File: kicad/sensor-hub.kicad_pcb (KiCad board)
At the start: 2 copper layers, 85 x 56 mm, 42 parts, among them J1 USB_B_Micro, J10 DHT22, J11 MQ_Sensors, J12 I2C-Si7021, J13 BG312L, J14 CC_DBG, J15 BT_DBG, J16 ZB_DBG, J17 CC_PWR, J5 ESP_TXD, J6 ESP_RXD, J7 DallasPullUp, J8 IRRecv/Dallas, J9 BH1750/Display, Q3 PN2222A, SW1 SW_Flash, U1 AP1117-33, U2 ESP-12F, U3 SZ1-CC2530, U5 CH330N

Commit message: Update kicad files
Signed-off-by: Zamir SUN <sztsian@gmail.com>
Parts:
- moved J10 6.22 mm to (277.7, 142.4)
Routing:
- net GND: track 203.9 -> 211.5 mm
- net DHT22: track 30.8 -> 37.0 mm
- net GPIO5: track 153.4 -> 156.3 mm
- net GPIO4: track 126.2 -> 129.0 mm
- net 3V3_MCU: track 386.4 -> 388.1 mm
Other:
- board text added: "Sensor Hub v0.3 by Zamir SUN"
- board text removed: "Sensor Hub v0.2 by Zamir SUN"

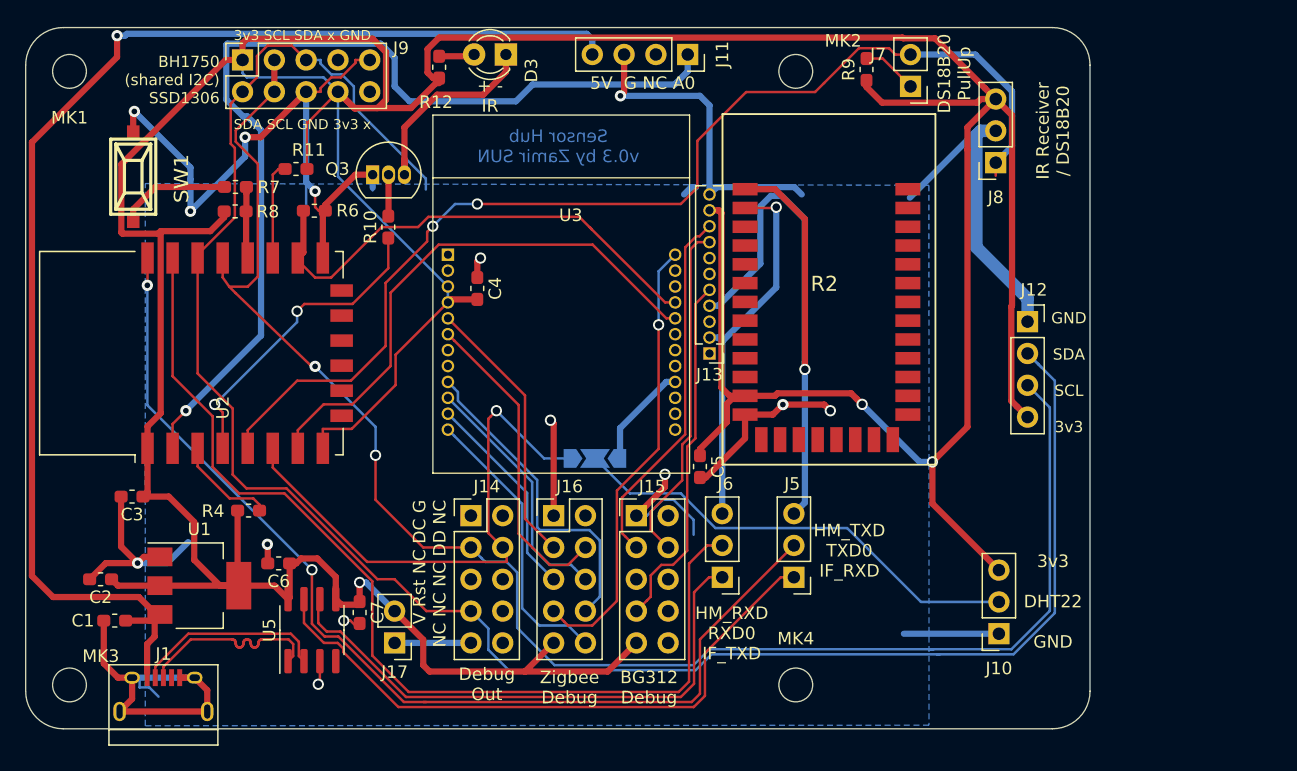
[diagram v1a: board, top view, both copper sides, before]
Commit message: WIP: v0.4 with pin order converter board
Signed-off-by: Zamir SUN <sztsian@gmail.com>
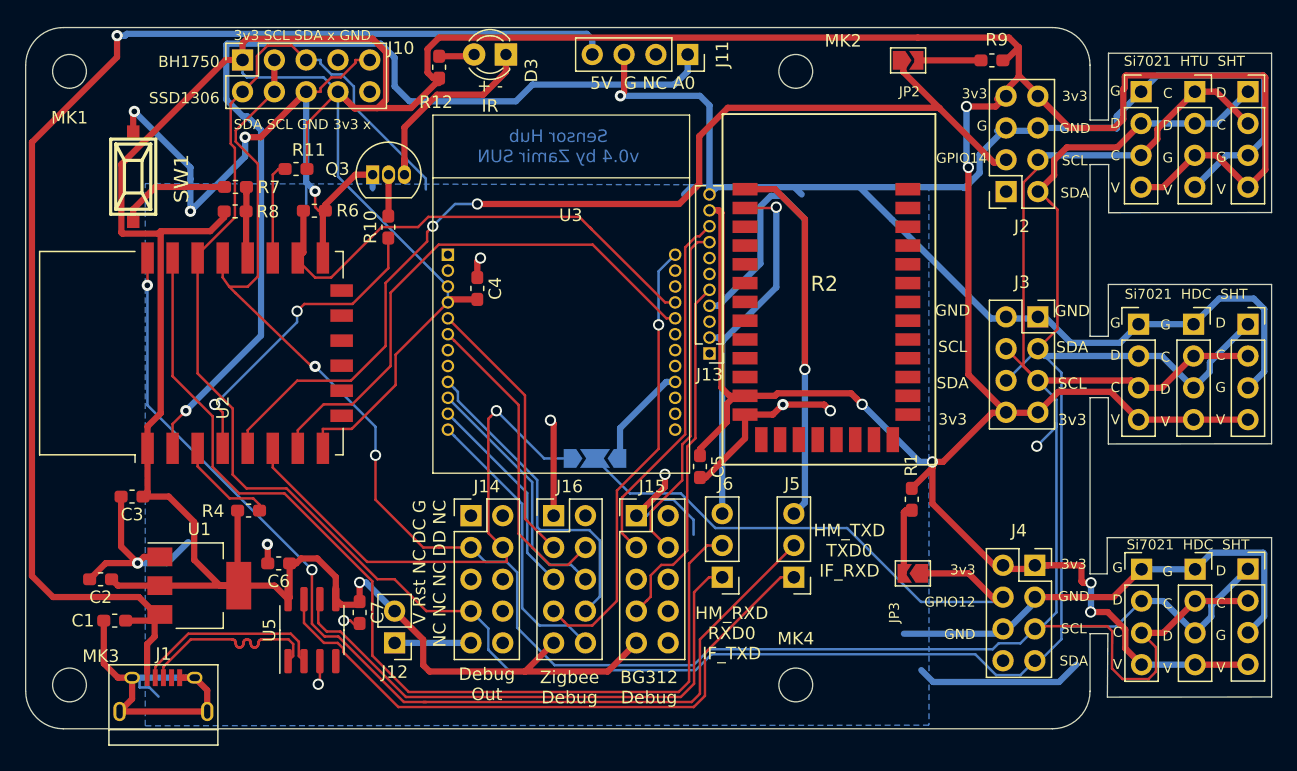
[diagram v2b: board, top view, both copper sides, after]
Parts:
- removed the J10 at (277.7, 142.4)
- removed the J12 at (280.0, 117.5)
- added J17: Si7021, Connector_PinHeader_2.54mm:PinHeader_1x04_P2.54mm_Vertical, F.Cu at (288.9, 117.7)
- added J18: HDC1080, Connector_PinSocket_2.54mm:PinSocket_1x04_P2.54mm_Vertical, F.Cu at (293.3, 117.7)
- added J19: SHT, Connector_PinSocket_2.54mm:PinSocket_1x04_P2.54mm_Vertical, F.Cu at (297.6, 117.7)
- added J2: IO14/SHT, Connector_PinSocket_2.54mm:PinSocket_2x04_P2.54mm_Vertical, F.Cu at (278.3, 107.1)
- added J20: Si7021, Connector_PinHeader_2.54mm:PinHeader_1x04_P2.54mm_Vertical, F.Cu at (289.1, 137.3)
- added J21: HDC1080, Connector_PinSocket_2.54mm:PinSocket_1x04_P2.54mm_Vertical, F.Cu at (293.4, 137.3)
- added J22: SHT, Connector_PinSocket_2.54mm:PinSocket_1x04_P2.54mm_Vertical, F.Cu at (297.6, 137.2)
- added J3: HDC/Si7021, Connector_PinSocket_2.54mm:PinSocket_2x04_P2.54mm_Vertical, F.Cu at (280.8, 117.1)
- added J4: IO12/SHT, Connector_PinSocket_2.54mm:PinSocket_2x04_P2.54mm_Vertical, F.Cu at (280.6, 136.9)
- added J9: SHT, Connector_PinSocket_2.54mm:PinSocket_1x04_P2.54mm_Vertical, F.Cu at (297.6, 99.1)
- added JP2: SJ_GPIO14, Jumper:SolderJumper-2_P1.3mm_Open_TrianglePad1.0x1.5mm, F.Cu at (270.5, 96.6)
- added JP3: SJ_GPIO12, Jumper:SolderJumper-2_P1.3mm_Open_TrianglePad1.0x1.5mm, F.Cu at (270.9, 137.6)
- added R1: 4.7k, Resistor_SMD:R_0603_1608Metric_Pad1.05x0.95mm_HandSolder, F.Cu at (270.8, 131.7)
- J7: value DallasPullUp -> Si7021; footprint Connector_PinHeader_2.54mm:PinHeader_1x02_P2.54mm_Vertical -> Connector_PinHeader_2.54mm:PinHeader_1x04_P2.54mm_Vertical
- J8: value IRRecv/Dallas -> HTU21D; footprint Connector_PinSocket_2.54mm:PinSocket_1x03_P2.54mm_Vertical -> Connector_PinSocket_2.54mm:PinSocket_1x04_P2.54mm_Vertical
- moved J7 18.4 mm to (289.1, 99.1), turned to 0 degrees
- moved J8 16.9 mm to (293.4, 99.1), turned to 0 degrees
- moved R9 10.0 mm to (277.2, 96.6), turned to 180 degrees
- renumbered J9 to J10, J17 to J12, JPe to JP1
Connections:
- J7 pad 1: Net-(J7-Pad1) -> GND
- J7 pad 2: GPIO14 -> GPIO5
- J8 pad 1: GPIO14 -> GPIO4
- J8 pad 2: GND -> GPIO5
- R9 pad 2: Net-(J7-Pad1) -> Net-(JP2-Pad2)
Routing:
- net GND: track 211.5 -> 318.1 mm
- net GPIO4: track 129.0 -> 218.6 mm, vias 2 -> 3
- net GPIO5: track 156.3 -> 236.1 mm
- net 3V3_MCU: track 388.1 -> 461.2 mm, vias 3 -> 7
- net GPIO14: track 89.7 -> 106.7 mm
- net (no net): track 0.00 -> 13.3 mm
- net DHT22: track 37.0 -> 43.8 mm
- net Net-(JP3-Pad2): track 0.00 -> 5.58 mm
- net Net-(JP2-Pad2): track 0.00 -> 5.09 mm
- net Net-(J7-Pad1): track 4.44 -> 0.00 mm
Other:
- board size 85 x 56 mm -> 99.5 x 56 mm
- board text added: "3v3 G GPIO14"
- board text added: "3v3 GND SCL SDA"
- board text added: "3v3 GPIO12 GND"
- board text added: "BH1750 SSD1306"
- board text added: "C D G V"
- board text added: "D C G V"
- board text added: "G C D V"
- board text added: "G D C V"
- board text added: "GND SCL SDA 3v3"
- board text added: "Sensor Hub v0.4 by Zamir SUN"
- board text added: "Si7021 HDC SHT"
- board text added: "Si7021 HTU SHT"
- board text removed: "3v3 DHT22 GND"
- board text removed: "BH1750 (shared I2C) SSD1306"
- board text removed: "DS18B20 PullUp"
- board text removed: "IR Receiver / DS18B20"
- board text removed: "Sensor Hub v0.3 by Zamir SUN"

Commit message: Finalize v0.4 version without pin converter board
Signed-off-by: Zamir SUN <sztsian@gmail.com>
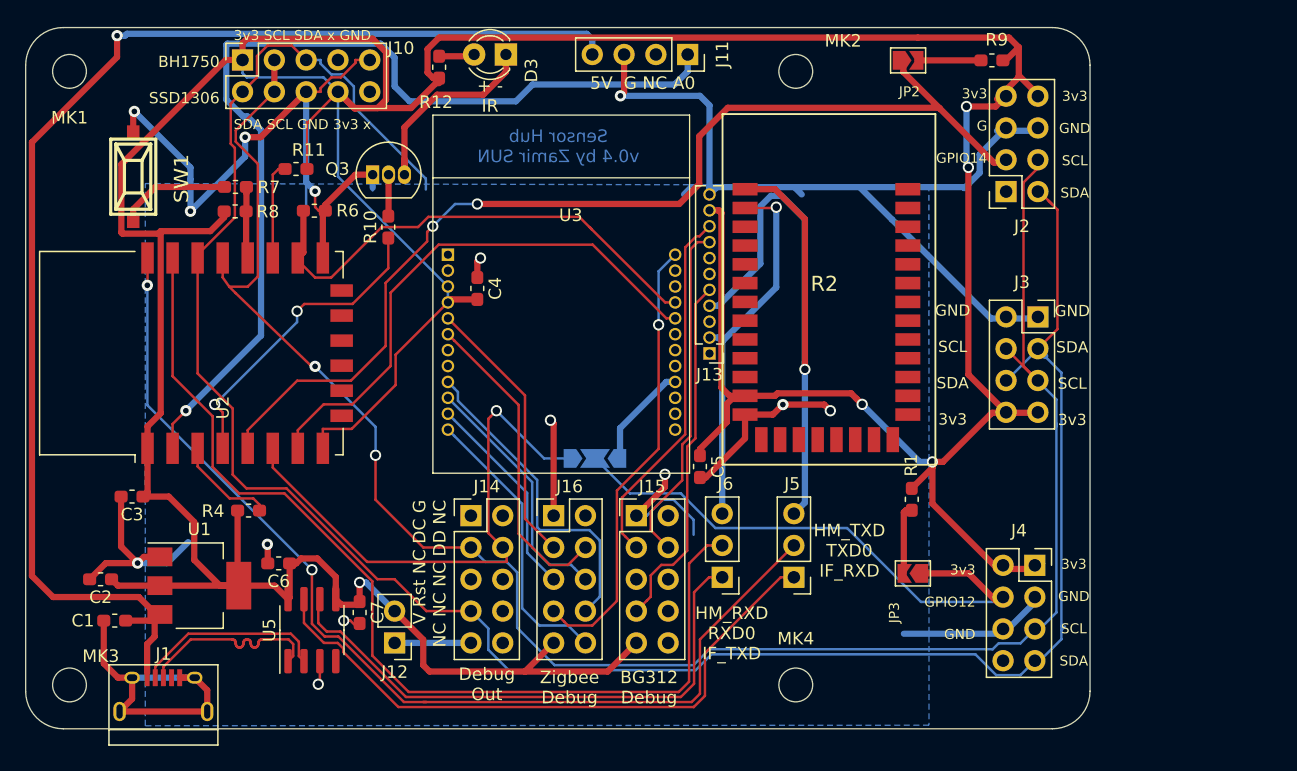
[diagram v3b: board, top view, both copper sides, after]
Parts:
- removed J17, J20, J7: Si7021, Connector_PinHeader_2.54mm:PinHeader_1x04_P2.54mm_Vertical
- removed J18, J21: HDC1080, Connector_PinSocket_2.54mm:PinSocket_1x04_P2.54mm_Vertical
- removed J19, J22, J9: SHT, Connector_PinSocket_2.54mm:PinSocket_1x04_P2.54mm_Vertical
- removed J8: HTU21D, Connector_PinSocket_2.54mm:PinSocket_1x04_P2.54mm_Vertical
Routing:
- net GND: track 318.1 -> 229.3 mm
- net 3V3_MCU: track 461.2 -> 374.3 mm, vias 7 -> 5
- net GPIO4: track 218.6 -> 152.0 mm, vias 3 -> 2
- net GPIO5: track 236.1 -> 176.4 mm
- net (no net): track 13.3 -> 0.00 mm
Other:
- board size 99.5 x 56 mm -> 85 x 56 mm
- board text removed: "C D G V"
- board text removed: "D C G V"
- board text removed: "G C D V"
- board text removed: "G D C V"
- board text removed: "Si7021 HDC SHT"
- board text removed: "Si7021 HTU SHT"
